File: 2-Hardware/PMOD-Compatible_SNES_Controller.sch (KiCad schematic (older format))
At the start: 5 parts, among them J1 PMOD_SINGLE, P1 CONN_1x7

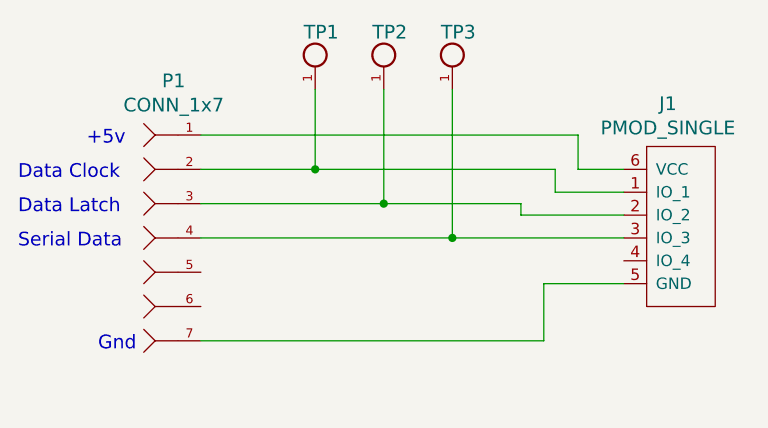
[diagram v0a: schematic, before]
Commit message: Rev'ed the board and added testpoint
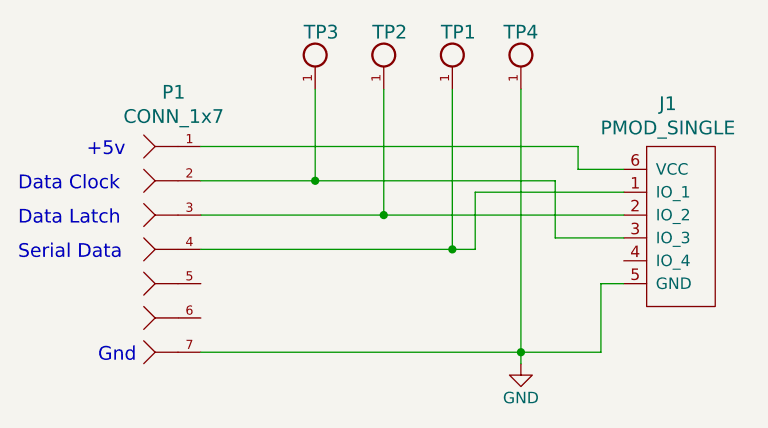
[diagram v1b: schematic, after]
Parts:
- added TP4: TEST_POINT, Connectors:TESTPOINT_063, symbol TEST_POINT
- TP1: renamed from TP3; DigikeyNumber (none) -> Value; Manufacturer (none) -> Value; ManufacturerNumber (none) -> Value
- TP3: renamed from TP1; DigikeyNumber (none) -> Value; Manufacturer (none) -> Value; ManufacturerNumber (none) -> Value
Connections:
- net at P1.2, TP3.1: now also J1.3 (IO_3); no longer J1.1 (IO_1)
- net at P1.4, TP1.1: now also J1.1 (IO_1); no longer J1.3 (IO_3)
- net GND: now reaches J1.5 (GND), P1.7
- net GND: now also TP4.1
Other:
- moved on the sheet: P1
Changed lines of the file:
@@
 LIBS:Sensors
 LIBS:TransistorParts
-EELAYER 26 0
+LIBS:power
+LIBS:PMOD-Compatible_SNES_Controller-cache
+EELAYER 25 0
 EELAYER END
 $Descr A4 11693 8268
 encoding utf-8
 Sheet 1 1
-Title ""
-Date ""
-Rev ""
+Title "PMOD-Compatible SNES Connector"
+Date "2016-12-28"
+Rev "A"
 Comp ""
 Comment1 ""
@@
 L CONN_1x7 P1
 U 1 1 582E97EE
-P 1950 3900
-F 0 "P1" H 2031 4587 60  0000 C CNN
-F 1 "CONN_1x7" H 2031 4481 60  0000 C CNN
-F 2 "Connectors:GAMING_SNES" H 1950 3900 60  0001 C CNN
-F 3 "" H 1950 3900 60  0000 C CNN
-	1    1950 3900
+P 1950 3950
+F 0 "P1" H 2031 4637 60  0000 C CNN
+F 1 "CONN_1x7" H 2031 4531 60  0000 C CNN
+F 2 "Connectors:GAMING_SNES" H 1950 3950 60  0001 C CNN
+F 3 "" H 1950 3950 60  0000 C CNN
+	1    1950 3950
 	1    0    0    -1
 $EndComp
-Text Notes 1650 3500 0    60   ~ 0
+Text Notes 1650 3550 0    60   ~ 0
 +5v
-Text Notes 1350 3650 0    60   ~ 0
+Text Notes 1350 3700 0    60   ~ 0
 Data Clock
-Text Notes 1350 3800 0    60   ~ 0
+Text Notes 1350 3850 0    60   ~ 0
 Data Latch
-Text Notes 1350 3950 0    60   ~ 0
+Text Notes 1350 4000 0    60   ~ 0
 Serial Data
-Text Notes 1700 4400 0    60   ~ 0
+Text Notes 1700 4450 0    60   ~ 0
 Gnd
 $Comp
@@
 	4000 3600 3800 3600
 Wire Wire Line
-	3800 3600 3800 3450
+	3800 3600 3800 3500
 Wire Wire Line
-	3800 3450 2150 3450
+	3800 3500 2150 3500
 Wire Wire Line
-	2150 3600 3700 3600
+	2150 3650 3700 3650
 Wire Wire Line
-	3700 3600 3700 3700
+	3700 3650 3700 3900
 Wire Wire Line
-	3700 3700 4000 3700
+	2150 3800 4000 3800
 Wire Wire Line
-	4000 3800 3550 3800
+	3550 3250 3550 4450
 Wire Wire Line
-	3550 3800 3550 3750
-Wire Wire Line
-	3550 3750 2150 3750
-Wire Wire Line
-	2150 3900 4000 3900
-Wire Wire Line
-	4000 4100 3650 4100
-Wire Wire Line
-	3650 4100 3650 4350
-Wire Wire Line
-	3650 4350 2150 4350
+	2150 4400 3900 4400
 $Comp
-L TEST_POINT TP1
+L TEST_POINT TP3
 U 1 1 582E9A25
 P 2650 3150
-F 0 "TP1" H 2600 3300 60  0000 L CNN
+F 0 "TP3" H 2600 3300 60  0000 L CNN
 F 1 "TEST_POINT" H 2650 3400 60  0001 C CNN
 F 2 "Connectors:TESTPOINT_063" H 2650 3150 60  0001 C CNN
 F 3 "" H 2650 3150 60  0000 C CNN
+F 4 "Value" H 2650 3150 60  0001 C CNN "DigikeyNumber"
+F 5 "Value" H 2650 3150 60  0001 C CNN "Manufacturer"
+F 6 "Value" H 2650 3150 60  0001 C CNN "ManufacturerNumber"
 	1    2650 3150
 	1    0    0    -1
@@
 $EndComp
 $Comp
-L TEST_POINT TP3
+L TEST_POINT TP1
 U 1 1 582E9B87
 P 3250 3150
-F 0 "TP3" H 3200 3300 60  0000 L CNN
+F 0 "TP1" H 3200 3300 60  0000 L CNN
 F 1 "TEST_POINT" H 3250 3400 60  0001 C CNN
 F 2 "Connectors:TESTPOINT_063" H 3250 3150 60  0001 C CNN
 F 3 "" H 3250 3150 60  0000 C CNN
+F 4 "Value" H 3250 3150 60  0001 C CNN "DigikeyNumber"
+F 5 "Value" H 3250 3150 60  0001 C CNN "Manufacturer"
+F 6 "Value" H 3250 3150 60  0001 C CNN "ManufacturerNumber"
 	1    3250 3150
 	1    0    0    -1
 $EndComp
 Wire Wire Line
-	2650 3250 2650 3600
-Connection ~ 2650 3600
+	2650 3250 2650 3650
+Connection ~ 2650 3650
 Wire Wire Line
-	2950 3250 2950 3750
-Connection ~ 2950 3750
+	2950 3250 2950 3800
+Connection ~ 2950 3800
 Wire Wire Line
-	3250 3250 3250 3900
-Connection ~ 3250 3900
+	3250 3250 3250 3950
+Connection ~ 3250 3950
+$Comp
+L TEST_POINT TP4
+U 1 1 58642EFF
+P 3550 3150
+F 0 "TP4" H 3550 3300 60  0000 C CNN
+F 1 "TEST_POINT" H 3550 3400 60  0001 C CNN
+F 2 "Connectors:TESTPOINT_063" H 3550 3150 60  0001 C CNN
+F 3 "" H 3550 3150 60  0000 C CNN
+	1    3550 3150
+	1    0    0    -1
+$EndComp
+$Comp
+L GND #PWR01
+U 1 1 586430D4
+P 3550 4450
+F 0 "#PWR01" H 3550 4200 50  0001 C CNN
+F 1 "GND" H 3550 4300 50  0000 C CNN
+F 2 "" H 3550 4450 50  0000 C CNN
+F 3 "" H 3550 4450 50  0000 C CNN
+	1    3550 4450
+	1    0    0    -1
+$EndComp
+Connection ~ 3550 4400
+Wire Wire Line
+	4000 4100 3900 4100
+Wire Wire Line
+	3900 4100 3900 4400
+Wire Wire Line
+	2150 3950 3350 3950
+Wire Wire Line
+	3700 3900 4000 3900
+Wire Wire Line
+	4000 3700 3350 3700
+Wire Wire Line
+	3350 3700 3350 3950
 $EndSCHEMATC
